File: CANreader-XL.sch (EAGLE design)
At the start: 77 parts, among them IC1 MCP2551, IC2 TJA1055T, IC3 BD9G101G, IC4 LM1117IMPX-3.3, IC5 STM32F107VBT, Q1 16MHz, SW1 SLEEP, SW2 TERM, U1 HC_05, X1 MINI-USB, X2 SWD, X3 GPIO, X4 UART, X5 CAN, X6 LAN

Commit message: Capacitor values
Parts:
- C10, C13, C17, C18, C20, C23, C25, C27, C4, C5, C6, C7, C8, C9: value 0.1 -> 0.1uF
- C3: value 0,1 -> 0.1uF
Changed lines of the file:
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@@
 <part name="C2" library="rcl" deviceset="C-EU" device="C0805" value="22pF"/>
 <part name="GND1" library="supply1" deviceset="GND" device=""/>
-<part name="C3" library="rcl" deviceset="C-EU" device="C0805" value="0,1"/>
-<part name="C4" library="rcl" deviceset="C-EU" device="C0805" value="0.1"/>
-<part name="C5" library="rcl" deviceset="C-EU" device="C0805" value="0.1"/>
-<part name="C6" library="rcl" deviceset="C-EU" device="C0805" value="0.1"/>
-<part name="C7" library="rcl" deviceset="C-EU" device="C0805" value="0.1"/>
-<part name="C8" library="rcl" deviceset="C-EU" device="C0805" value="0.1"/>
+<part name="C3" library="rcl" deviceset="C-EU" device="C0805" value="0.1uF"/>
+<part name="C4" library="rcl" deviceset="C-EU" device="C0805" value="0.1uF"/>
+<part name="C5" library="rcl" deviceset="C-EU" device="C0805" value="0.1uF"/>
+<part name="C6" library="rcl" deviceset="C-EU" device="C0805" value="0.1uF"/>
+<part name="C7" library="rcl" deviceset="C-EU" device="C0805" value="0.1uF"/>
+<part name="C8" library="rcl" deviceset="C-EU" device="C0805" value="0.1uF"/>
 <part name="+3V1" library="supply1" deviceset="+3V3" device=""/>
 <part name="IC2" library="STM32_CAN-USB" deviceset="TJA1054T" device="" value="TJA1055T"/>
@@
 <part name="R4" library="rcl" deviceset="R-EU_" device="R0805" value="1K"/>
 <part name="GND3" library="supply1" deviceset="GND" device=""/>
-<part name="C9" library="rcl" deviceset="C-EU" device="C0805" value="0.1"/>
+<part name="C9" library="rcl" deviceset="C-EU" device="C0805" value="0.1uF"/>
 <part name="GND4" library="supply1" deviceset="GND" device=""/>
 <part name="+3V2" library="supply1" deviceset="+3V3" device=""/>
 <part name="R5" library="rcl" deviceset="R-EU_" device="R0805" value="3K3"/>
-<part name="C10" library="rcl" deviceset="C-EU" device="C0805" value="0.1"/>
+<part name="C10" library="rcl" deviceset="C-EU" device="C0805" value="0.1uF"/>
 <part name="P+2" library="supply1" deviceset="+5V" device=""/>
 <part name="+3V4" library="supply1" deviceset="+3V3" device=""/>
@@
 <part name="GND7" library="supply1" deviceset="GND" device=""/>
 <part name="R8" library="rcl" deviceset="R-EU_" device="R0805" value="3.9K"/>
-<part name="C13" library="rcl" deviceset="C-EU" device="C0805" value="0.1"/>
+<part name="C13" library="rcl" deviceset="C-EU" device="C0805" value="0.1uF"/>
 <part name="P+3" library="supply1" deviceset="+12V" device=""/>
 <part name="GND8" library="supply1" deviceset="GND" device=""/>
@@
 <part name="P+5" library="supply1" deviceset="+5V" device=""/>
 <part name="X1" library="STM32_CAN-USB" deviceset="MINI-USB-" device="UX60-MB-5ST" value="MINI-USB"/>
-<part name="C17" library="rcl" deviceset="C-EU" device="C0805" value="0.1"/>
-<part name="C18" library="rcl" deviceset="C-EU" device="C0805" value="0.1"/>
+<part name="C17" library="rcl" deviceset="C-EU" device="C0805" value="0.1uF"/>
+<part name="C18" library="rcl" deviceset="C-EU" device="C0805" value="0.1uF"/>
 <part name="P+6" library="supply1" deviceset="+5V" device=""/>
 <part name="GND11" library="supply1" deviceset="GND" device=""/>
@@
 <part name="DR1" library="STM32_CAN-USB" deviceset="CDRH127" device="" value="CDRH127 100u"/>
 <part name="C19" library="rcl" deviceset="C-EU" device="C0805" value="1nF"/>
-<part name="C20" library="rcl" deviceset="C-EU" device="C0805" value="0.1"/>
+<part name="C20" library="rcl" deviceset="C-EU" device="C0805" value="0.1uF"/>
 <part name="C21" library="rcl" deviceset="C-EU" device="C0805" value="4.7uF"/>
 <part name="C22" library="rcl" deviceset="C-EU" device="C0805" value="1nF"/>
-<part name="C23" library="rcl" deviceset="C-EU" device="C0805" value="0.1"/>
+<part name="C23" library="rcl" deviceset="C-EU" device="C0805" value="0.1uF"/>
 <part name="C24" library="rcl" deviceset="C-EU" device="C0805" value="4.7uF"/>
 <part name="GND14" library="supply1" deviceset="GND" device=""/>
@@
 <part name="U1" library="Bluetooth HC-05" deviceset="HC_05" device=""/>
 <part name="GND21" library="supply1" deviceset="GND" device=""/>
-<part name="C25" library="rcl" deviceset="C-EU" device="C0805" value="0.1"/>
+<part name="C25" library="rcl" deviceset="C-EU" device="C0805" value="0.1uF"/>
 <part name="+3V5" library="supply1" deviceset="+3V3" device=""/>
 <part name="R13" library="rcl" deviceset="R-EU_" device="R0805" value="470"/>
@@
 <part name="GND25" library="supply1" deviceset="GND" device=""/>
 <part name="+3V13" library="supply1" deviceset="+3V3" device=""/>
-<part name="C27" library="rcl" deviceset="C-EU" device="C0805" value="0.1"/>
+<part name="C27" library="rcl" deviceset="C-EU" device="C0805" value="0.1uF"/>
 <part name="GND33" library="supply1" deviceset="GND" device=""/>
 <part name="GND34" library="supply1" deviceset="GND" device=""/>

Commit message: Minor fixes
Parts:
- IC2: value TJA1055T -> TJA1055T/3
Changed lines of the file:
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@@
 <part name="C8" library="rcl" deviceset="C-EU" device="C0805" value="0.1uF"/>
 <part name="+3V1" library="supply1" deviceset="+3V3" device=""/>
-<part name="IC2" library="STM32_CAN-USB" deviceset="TJA1054T" device="" value="TJA1055T"/>
+<part name="IC2" library="STM32_CAN-USB" deviceset="TJA1054T" device="" value="TJA1055T/3"/>
 <part name="R1" library="rcl" deviceset="R-EU_" device="R0805" value="5.6K"/>
 <part name="R2" library="rcl" deviceset="R-EU_" device="R0805" value="5.6K"/>

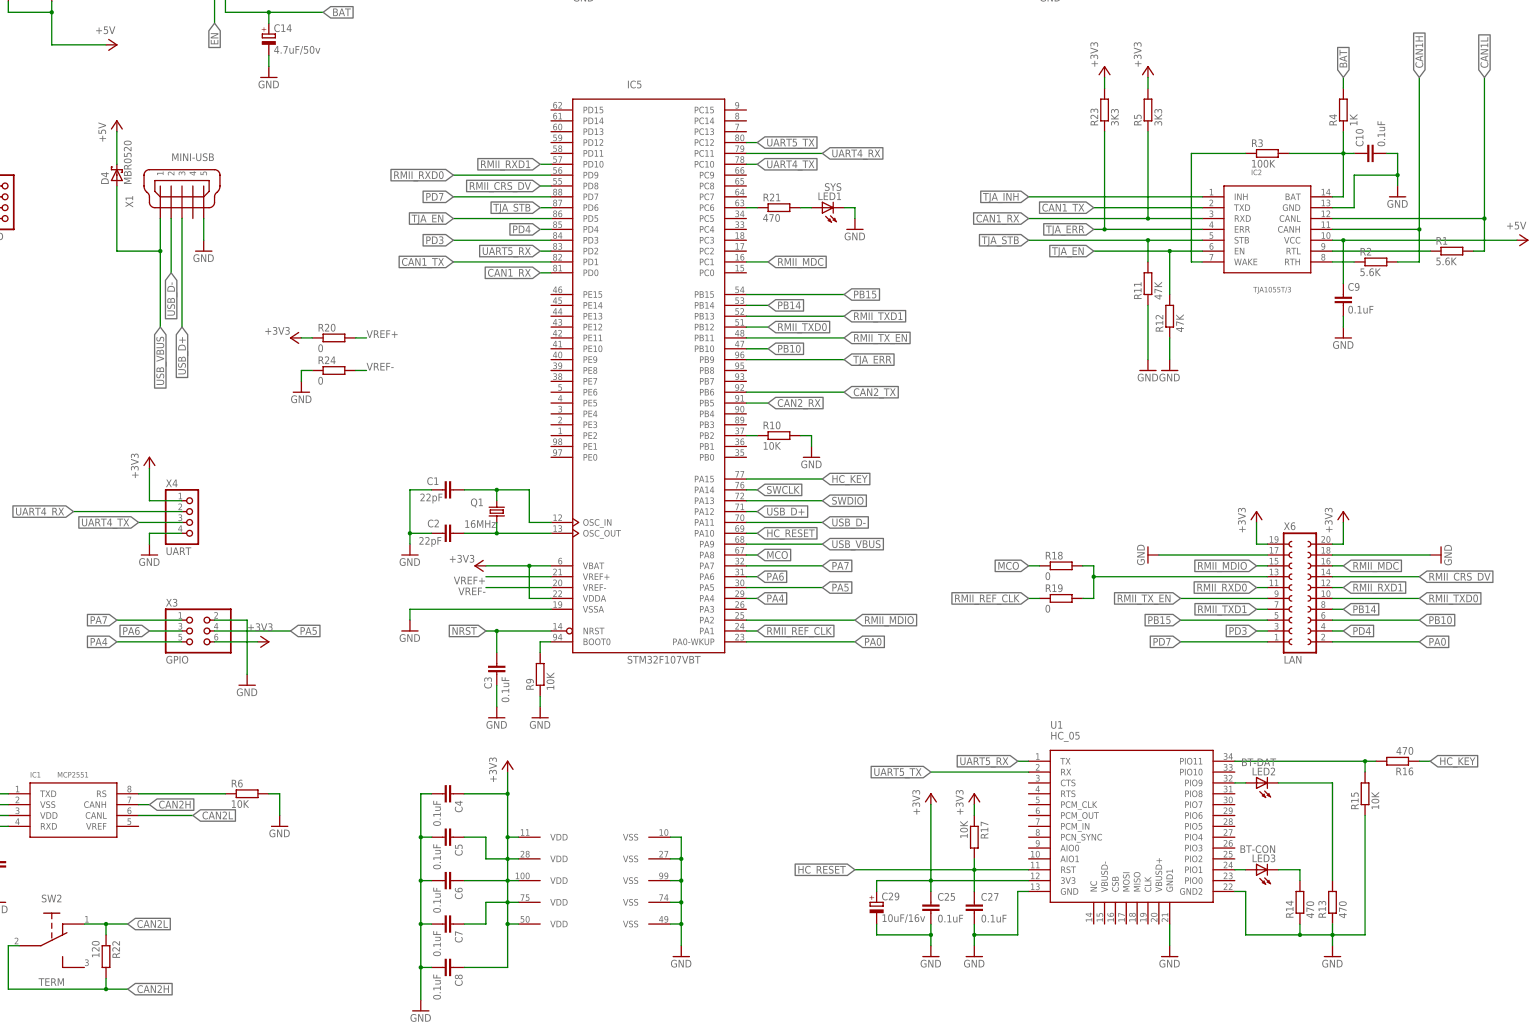
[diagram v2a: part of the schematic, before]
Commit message: LQFP100 -> LQFP64 in schematics
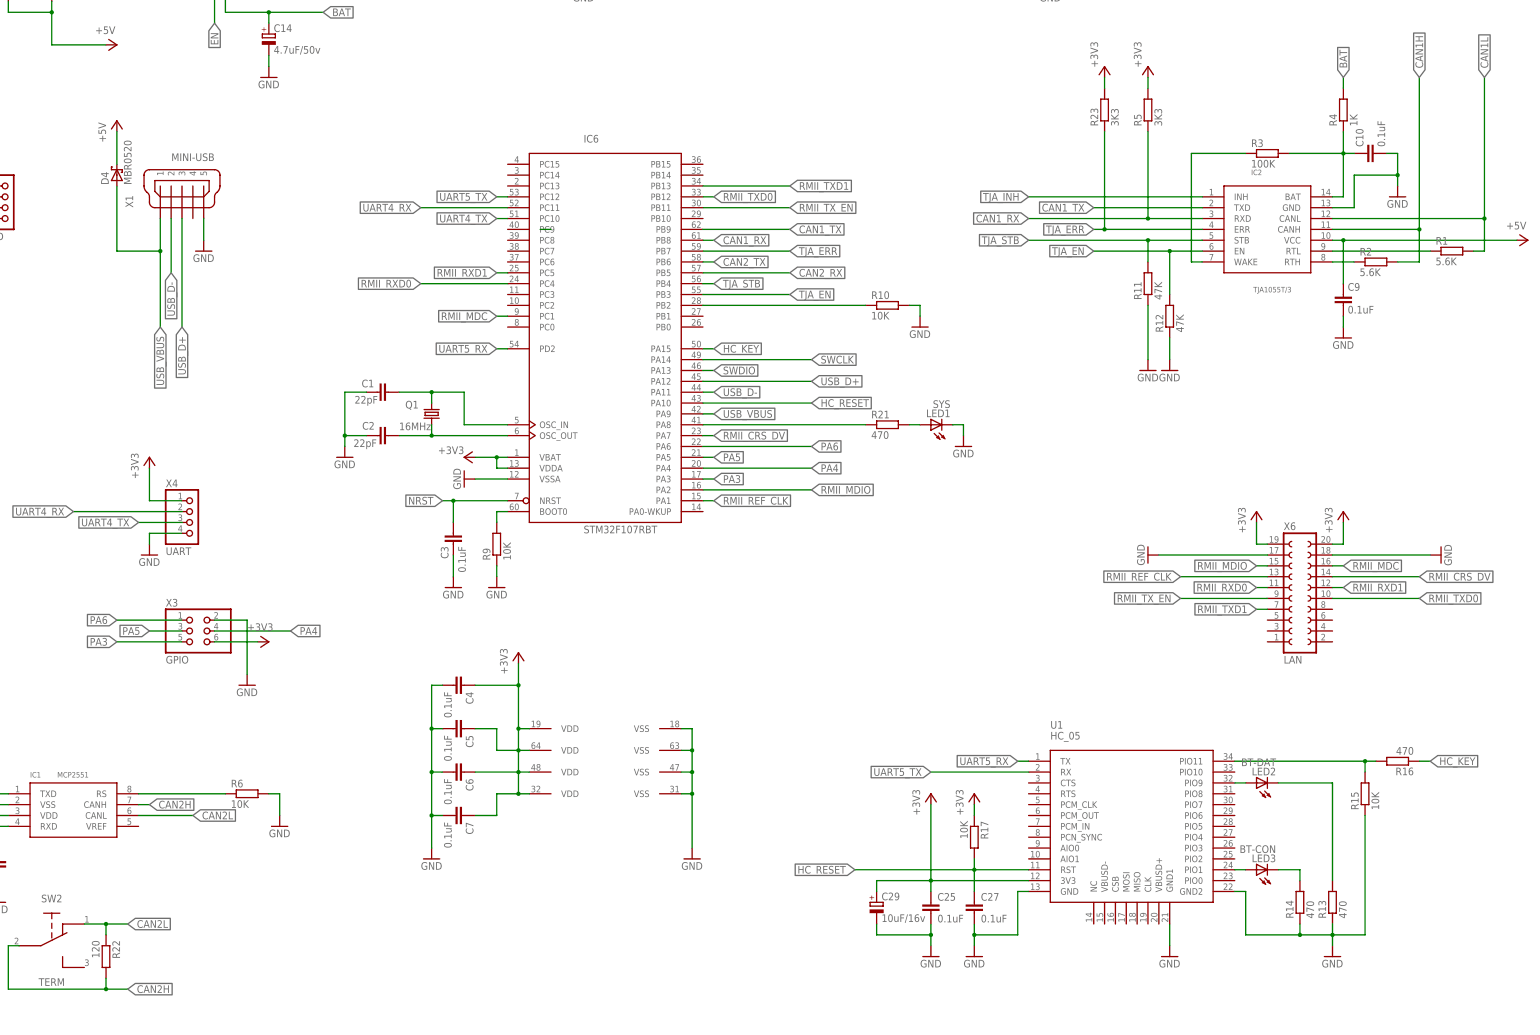
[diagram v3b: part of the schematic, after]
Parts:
- removed C8: 0.1uF, rcl:C-EUC0805
- removed IC5: STM32F107VBT, micro-stm_v2:STM32F107VBT
- removed R18, R19, R20, R24: 0, rcl:R-EU_R0805
- added IC6: STM32F107RBT, micro-stm_v2:STM32F107RBT
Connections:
- removed net MCO: IC5MCU.PA8, R18.1
- removed net N$37: R18.2, R19.2, X6.13
- removed net PA0: IC5MCU.PA0-WKUP, X6.2
- removed net PA7: IC5MCU.PA7, X3.1
- removed net PB10: IC5MCU.PB10, X6.6
- removed net PB14: IC5MCU.PB14, X6.8
- removed net PB15: IC5MCU.PB15, X6.5
- removed net PD3: IC5MCU.PD3, X6.3
- removed net PD4: IC5MCU.PD4, X6.4
- removed net PD7: IC5MCU.PD7, X6.1
- removed net VREF+: IC5MCU.VREF+, R20.2
- removed net VREF-: IC5MCU.VREF-, R24.2
- new net PA3: IC6MCU.PA3, X3.5
- net +3V3: now also IC6MCU.VBAT, IC6MCU.VDDA, IC6PWR.VDD@1, IC6PWR.VDD@2, IC6PWR.VDD@3, IC6PWR.VDD@4; no longer C8.1, IC5MCU.VBAT, IC5MCU.VDDA, IC5PWR.VDD@1, IC5PWR.VDD@2, IC5PWR.VDD@3, IC5PWR.VDD@4, IC5PWR.VDD@5, R20.1
- net CAN1_RX: now also IC6MCU.PB8; no longer IC5MCU.PD0
- net CAN1_TX: now also IC6MCU.PB9; no longer IC5MCU.PD1
- net CAN2_RX: now also IC6MCU.PB5; no longer IC5MCU.PB5
- net CAN2_TX: now also IC6MCU.PB6; no longer IC5MCU.PB6
- net GND: now also IC6MCU.VSSA, IC6PWR.VSS@1, IC6PWR.VSS@2, IC6PWR.VSS@3, IC6PWR.VSS@4; no longer C8.2, IC5MCU.VSSA, IC5PWR.VSS@1, IC5PWR.VSS@2, IC5PWR.VSS@3, IC5PWR.VSS@4, IC5PWR.VSS@5, R24.1
- net HC_KEY: now also IC6MCU.PA15; no longer IC5MCU.PA15
- net HC_RESET: now also IC6MCU.PA10; no longer IC5MCU.PA10
- net N$1: now also IC6MCU.OSC_IN; no longer IC5MCU.OSC_IN
- net N$2: now also IC6MCU.OSC_OUT; no longer IC5MCU.OSC_OUT
- net N$3: now also IC6MCU.BOOT0; no longer IC5MCU.BOOT0
- net N$4: now also IC6MCU.PB2; no longer IC5MCU.PB2
- net N$6: now also IC6MCU.PA8; no longer IC5MCU.PC6
- net NRST: now also IC6MCU.NRST; no longer IC5MCU.NRST
- net PA4: now also IC6MCU.PA4, X3.4; no longer IC5MCU.PA4, X3.5
- net PA5: now also IC6MCU.PA5, X3.3; no longer IC5MCU.PA5, X3.4
- net PA6: now also IC6MCU.PA6, X3.1; no longer IC5MCU.PA6, X3.3
- net RMII_CRS_DV: now also IC6MCU.PA7; no longer IC5MCU.PD8
- net RMII_MDC: now also IC6MCU.PC1; no longer IC5MCU.PC1
- net RMII_MDIO: now also IC6MCU.PA2; no longer IC5MCU.PA2
- net RMII_REF_CLK: now also IC6MCU.PA1, X6.13; no longer IC5MCU.PA1, R19.1
- net RMII_RXD0: now also IC6MCU.PC4; no longer IC5MCU.PD9
- net RMII_RXD1: now also IC6MCU.PC5; no longer IC5MCU.PD10
- net RMII_TXD0: now also IC6MCU.PB12; no longer IC5MCU.PB12
- net RMII_TXD1: now also IC6MCU.PB13; no longer IC5MCU.PB13
- net RMII_TX_EN: now also IC6MCU.PB11; no longer IC5MCU.PB11
- net SWCLK: now also IC6MCU.PA14; no longer IC5MCU.PA14
- net SWDIO: now also IC6MCU.PA13; no longer IC5MCU.PA13
- net TJA_EN: now also IC6MCU.PB3; no longer IC5MCU.PD5
- net TJA_ERR: now also IC6MCU.PB7; no longer IC5MCU.PB9
- net TJA_STB: now also IC6MCU.PB4; no longer IC5MCU.PD6
- net UART4_RX: now also IC6MCU.PC11; no longer IC5MCU.PC11
- net UART4_TX: now also IC6MCU.PC10; no longer IC5MCU.PC10
- net UART5_RX: now also IC6MCU.PD2; no longer IC5MCU.PD2
- net UART5_TX: now also IC6MCU.PC12; no longer IC5MCU.PC12
- net USB_D+: now also IC6MCU.PA12; no longer IC5MCU.PA12
- net USB_D-: now also IC6MCU.PA11; no longer IC5MCU.PA11
- net USB_VBUS: now also IC6MCU.PA9; no longer IC5MCU.PA9
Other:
- moved on the sheet: C1, C2, C3, C4, C5, C6, C7, LED1, Q1, R10, R21, R9

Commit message: Ethernet initial
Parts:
- added C28, C30, C32, C33, C34, C36, C37, C8: 0.1uF, rcl:C-EUC0805
- added C31: 0.01uF, rcl:C-EUC0805
- added C35: 10uF, rcl:C-EUC0805
- added C38, C39: 1uF, rcl:C-EUC0805
- added IC7: DP83848I, STM32_CAN-USB:DP83848I
- added QG1: 50MHz, crystal:SM77H
- added R18: 10K, rcl:R-EU_R0805
- added R19, R20, R30, R31: 2K2, rcl:R-EU_R0805
- added R24, R25, R26, R27, R34: 18, rcl:R-EU_R0805
- added R28, R29: 330, rcl:R-EU_R0805
- added R32: 4K7, rcl:R-EU_R0805
- added R33: 150, rcl:R-EU_R0805
- added X7: J11012F21K, con-pulse:J11012F21K
- Q1: value 16MHz -> 25MHz
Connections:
- new net LEDACT_LINK: IC7.LED_ACT/COL/AN_EN, R28.2
- new net LED_LINK: IC7.LED_LNK/AN0, R29.2
- new net N$16: IC7.RESET_N, R18.1
- new net N$17: IC7.RESERVED2, R30.1
- new net N$20: IC7.RX_DV/MDII_MODE, R20.2
- new net N$21: IC7.RESERVED1, R31.1
- new net N$22: R28.1, X7.C-R
- new net N$23: R29.1, X7.C-L
- new net N$24: IC7.X1, QG1.OUT
- new net N$26: IC7.RBIAS, R32.1
- new net N$27: R32.2, R33.2
- new net N$28: R33.1, R34.1
- new net PFB: C32.1, C33.1, C34.1, C35.1, IC7.PFBIN1, IC7.PFBIN2, IC7.PFBOUT
- new net RD+: IC7.RD+, R26.2, X7.RD+
- new net RD-: IC7.RD-, R27.1, X7.RD-
- new net TD+: IC7.TD+, R24.2, X7.TD+
- new net TD-: IC7.TD-, R25.1, X7.TD-
- net +3V3: now also C28.1, C30.1, C31.1, C36.1, C37.1, C38.1, C39.1, C8.1, IC7.AVDD33, IC7.IOVDD33_1, IC7.IOVDD33_2, QG1.VCC, R18.2, R19.1, R20.1, R24.1, R25.2, R26.1, R27.2, R30.2, R31.2, X7.A-L, X7.A-R, X7.CR, X7.CT
- net GND: now also C28.2, C30.2, C31.2, C32.2, C33.2, C34.2, C35.2, C36.2, C37.2, C38.2, C39.2, C8.2, IC7.AGND1, IC7.AGND2, IC7.DGND, IC7.IOGND1, IC7.IOGND2, QG1.GND, R34.2, X7.8
- net RMII_CRS_DV: now also IC7.CRS/CRS_DV/LED_CFG, R19.2
- net RMII_MDC: now also IC7.MDC
- net RMII_MDIO: now also IC7.MDIO
- net RMII_RXD0: now also IC7.RXD_0/PHYAD1, IC7.RXD_1/PHYAD2
- net RMII_TXD0: now also IC7.TXD_0
- net RMII_TXD1: now also IC7.TXD_1
- net RMII_TX_EN: now also IC7.TX_EN
